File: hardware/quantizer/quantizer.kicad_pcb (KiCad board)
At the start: 2 copper layers, 105.7 x 100 mm, 96 parts, among them J1 Power, J10 Transpose, J11 TRIGGER IN B, J12 g, J13 g, J14 g, J15 g, J16 g, J17 g, J18 g, J19 g, J2 CV IN A, J20 g, J21 g, J22 g, J23 g, J24 g, J25 g, J26 g, J27 g, J28 g, J29 g, J3 CV IN B, J30 g, J31 g, J32 g, J33 g, J34 g, J35 g, J36 g, J37 g, J38 g, J39 g, J4 CV OUT A, J40 g, J41 g, J42 g, J43 g, J5 CV OUT B, J6 TRIGGER OUT A, J7 TRIGGER OUT B, J8 Portamento, J9 TRIGGER IN A, Q1 2N3904, Q2 2N3904, Q3 2N3904, Q4 2N3904, SW1 Rotary_Encoder_Switch, U2 MCP4921, U3 MCP4921, U4 TL072, U5 TL431LP

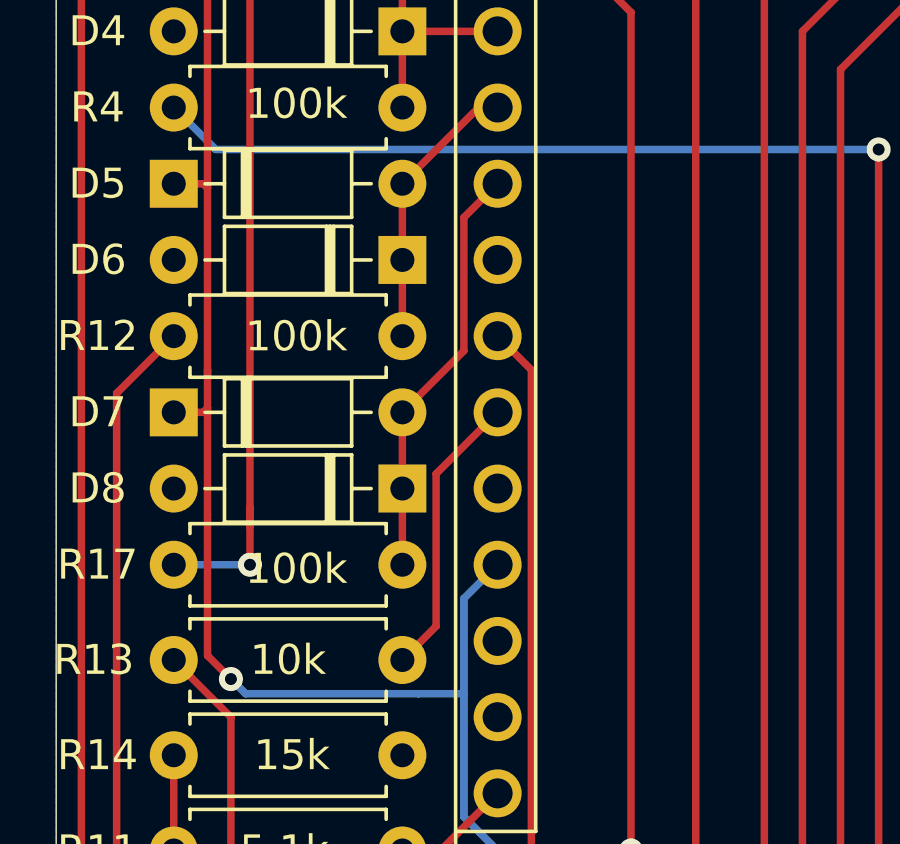
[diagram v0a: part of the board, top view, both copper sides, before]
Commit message: Updated brd/sch pin change, added photos
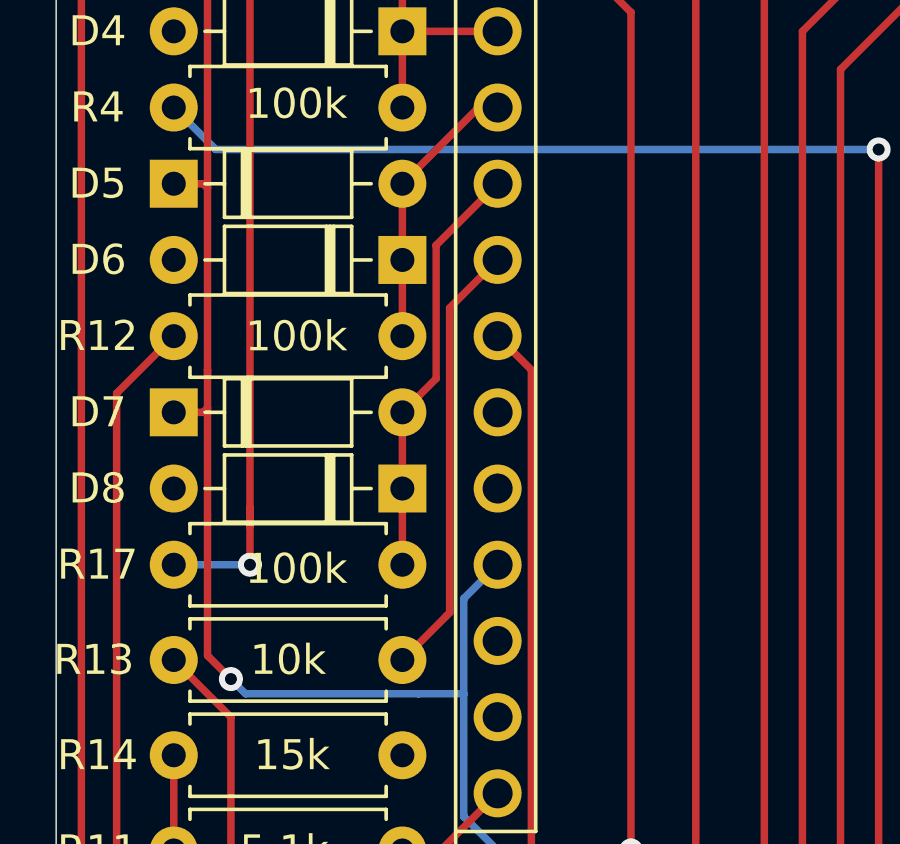
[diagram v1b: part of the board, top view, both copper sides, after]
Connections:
- A1 pad 23: Net-(A1-Pad23) -> TGR_OUT_B
- A1 pad 25: TGR_OUT_B -> Net-(A1-Pad25)
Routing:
- net TGR_OUT_B: track 9.57 -> 14.7 mm
